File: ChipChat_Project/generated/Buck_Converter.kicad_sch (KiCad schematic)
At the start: 4 parts

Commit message: 💾 snapshot 2026-02-23_00-19-22
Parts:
- added L1: 1.0uH, symbol L
- added U1: TPS628438DRL, symbol TPS628436DRL
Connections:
- net Buck_Vset_3V3: now also U1.3 (VSET)
- net GND: now also U1.1 (GND)
- net PP_3V3_OUT: now also L1.1, U1.6 (VOS)
- net PP_5V_SYS: now also U1.2 (VIN), U1.4 (EN)
- new net BUCK_SW: L1.2, U1.5 (SW)

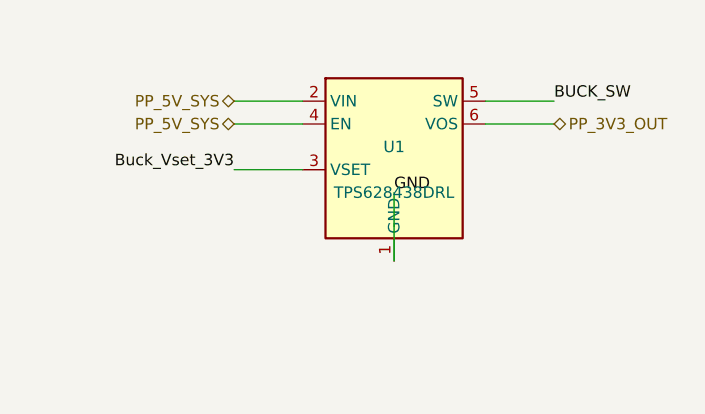
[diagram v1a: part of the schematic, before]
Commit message: finished basic full schematic generation from json, next follow and implement llm_integration.md
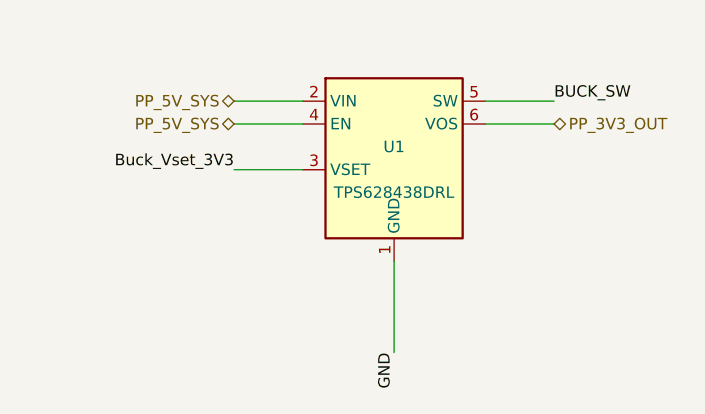
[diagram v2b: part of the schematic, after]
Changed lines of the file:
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@@
 	(wire
 		(pts
-			(xy 200.0 110.16) (xy 200.0 102.54)
+			(xy 200.0 110.16) (xy 200.0 120.32)
 		)
 		(stroke
@@
 	)
 	(label "GND"
-		(at 200.0 102.54 0)
+		(at 200.0 120.32 90)
 		(effects
 			(font
 				(size 1.27 1.27)
 			)
-			(justify left bottom)
+			(justify right bottom)
 		)
 	)
